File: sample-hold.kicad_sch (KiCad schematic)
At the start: 76 parts, among them J1 Conn_02x05_Odd_Even, J2 AudioJack2_SwitchT, J3 AudioJack2_SwitchT, J4 AudioJack2_SwitchT, J5 AudioJack2_SwitchT, Q1 BC547C, Q2 BCM847, Q3 MMBF4393, SW1 ON-ON-ON, U1 TL074, U2 TL074

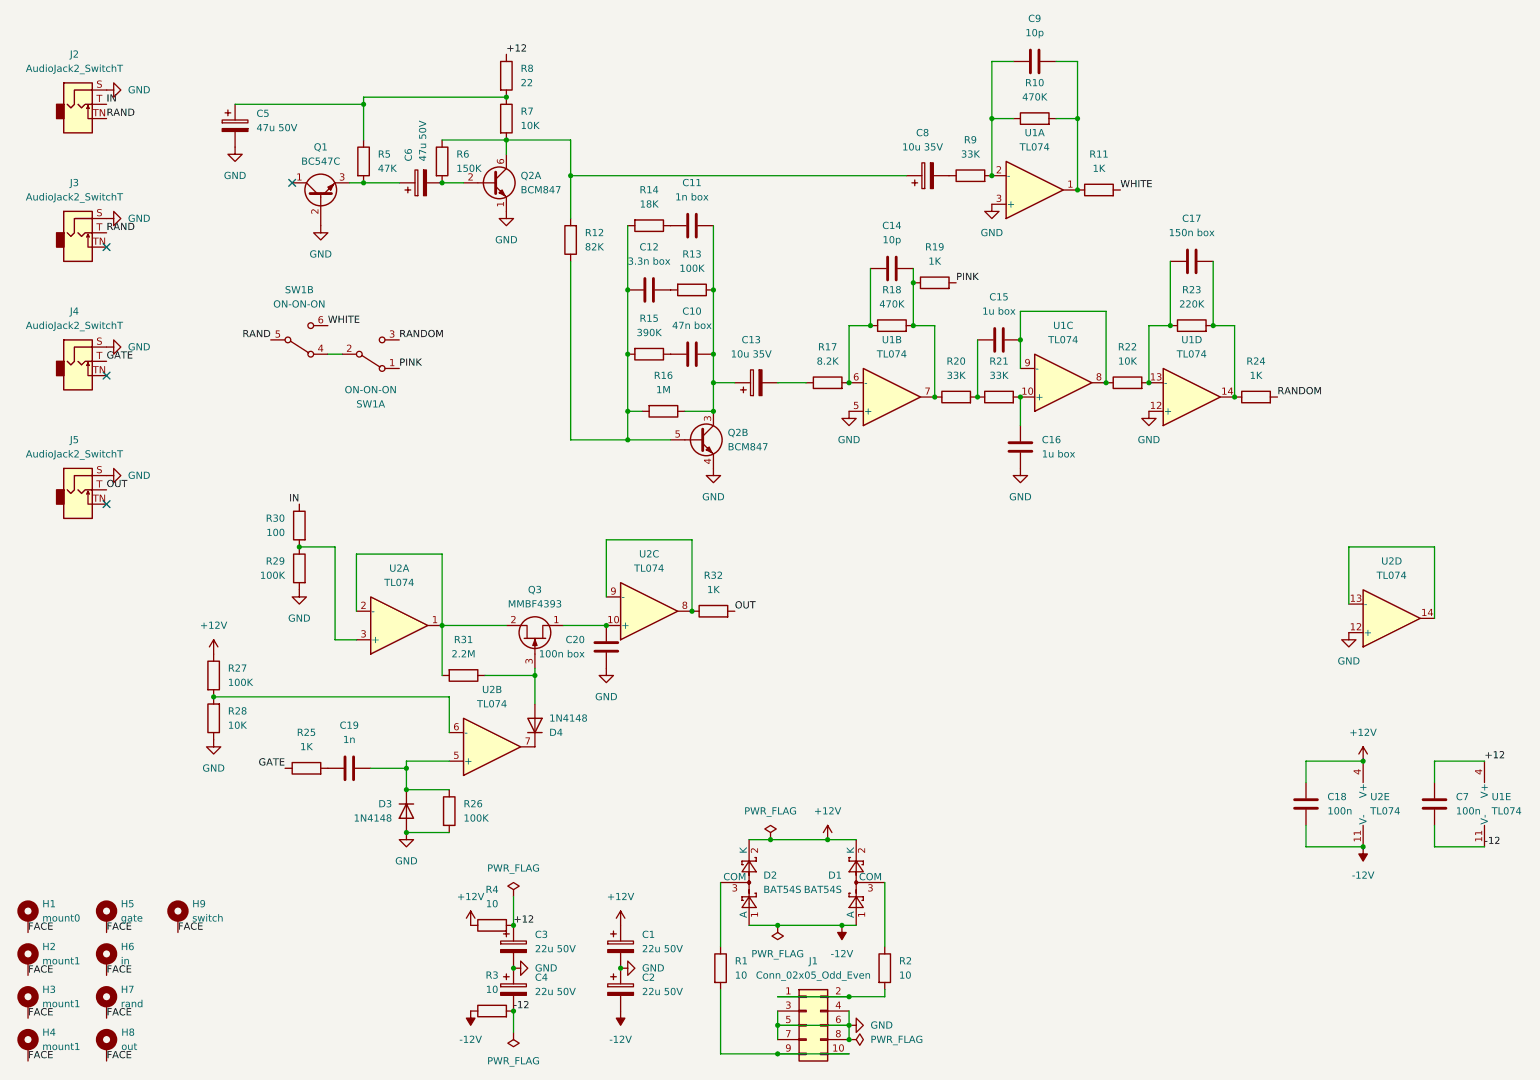
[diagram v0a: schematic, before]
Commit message: adding rate knob and internal clock
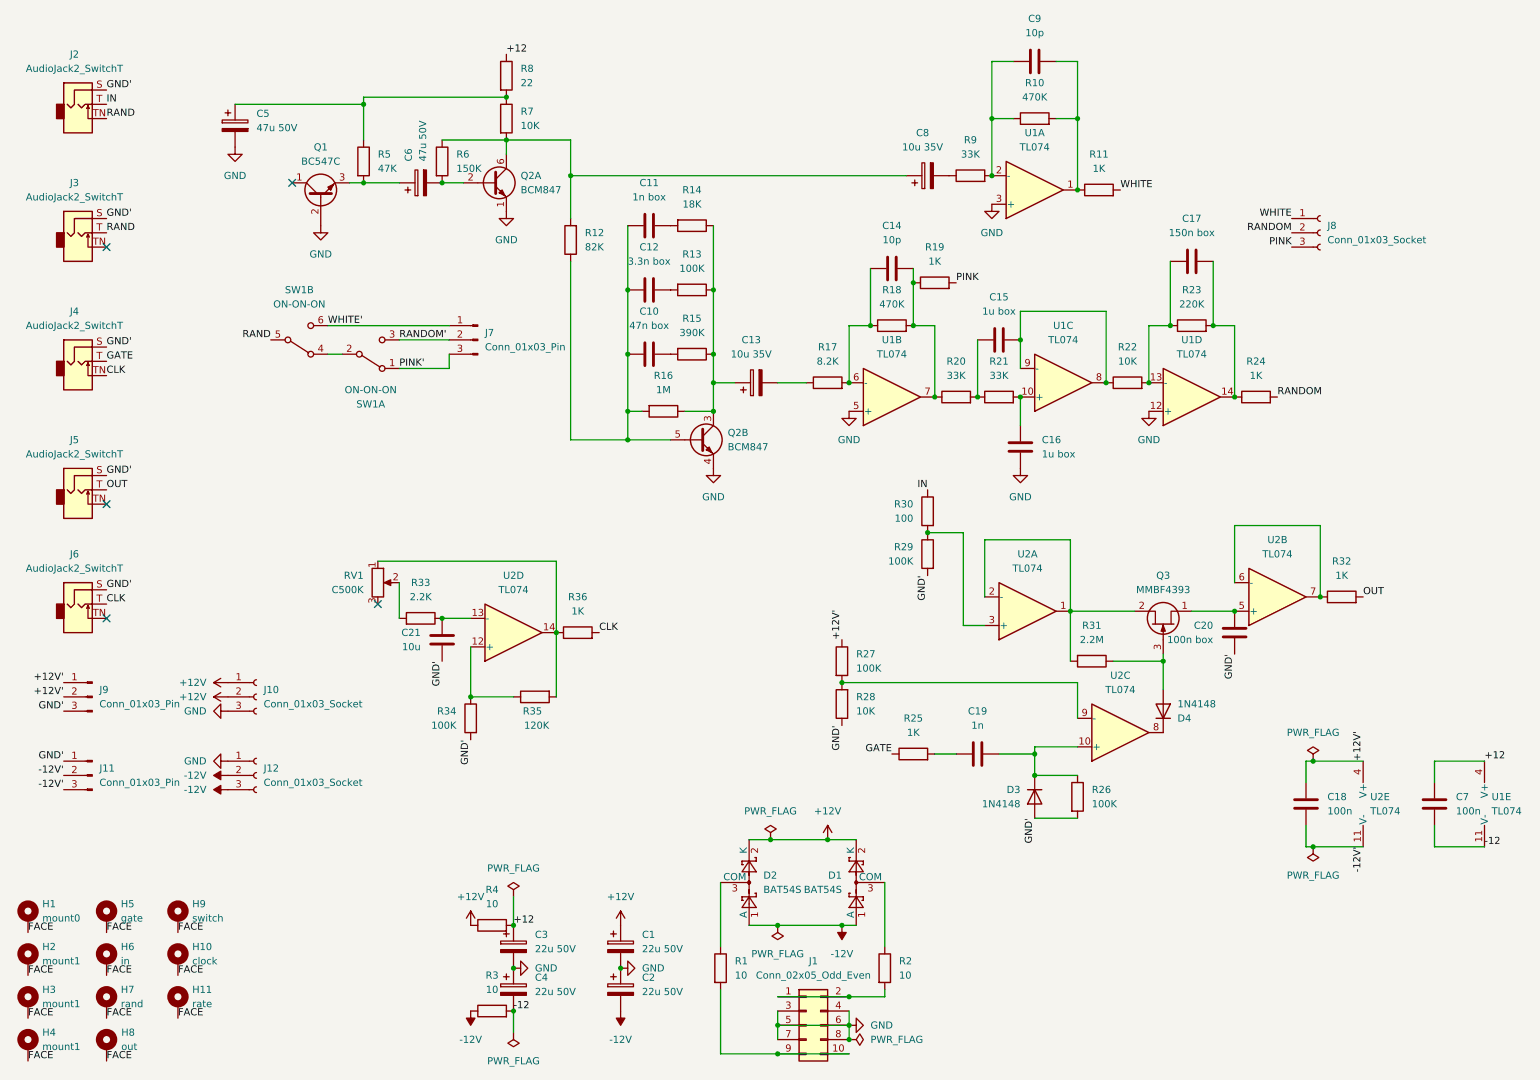
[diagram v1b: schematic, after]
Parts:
- added C21: 10u, Capacitor_SMD:C_0805_2012Metric, symbol Device:C
- added H10: clock, Eurorack:Mech-AudioJack-Hole-Output-Clock, symbol Mechanical:MountingHole_Pad
- added H11: rate, Eurorack:Mech-Potentiometer-Hole_level_90deg, symbol Mechanical:MountingHole_Pad
- added J10, J12, J8: Conn_01x03_Socket, Connector_PinSocket_2.54mm:PinSocket_1x03_P2.54mm_Vertical, symbol Connector:Conn_01x03_Socket
- added J11, J7, J9: Conn_01x03_Pin, Connector_PinHeader_2.54mm:PinHeader_1x03_P2.54mm_Vertical, symbol Connector:Conn_01x03_Pin
- added J6: AudioJack2_SwitchT, Eurorack:AudioJack2_Tayda_A-2566, symbol Eurorack:AudioJack2_SwitchT
- added R33: 2.2K, Resistor_SMD:R_0805_2012Metric, symbol Device:R
- added R34: 100K, Resistor_SMD:R_0805_2012Metric, symbol Device:R
- added R35: 120K, Resistor_SMD:R_0805_2012Metric, symbol Device:R
- added R36: 1K, Resistor_SMD:R_0805_2012Metric, symbol Device:R
- added RV1: C500K, Eurorack:Potentiometer_RV16AF-41-15R1, symbol Device:R_Potentiometer
- C11: footprint Capacitor_THT:C_Rect_L7.2mm_W5.5mm_P5.00mm_FKS2_FKP2_MKS2_MKP2 -> Capacitor_THT:C_Rect_L7.2mm_W2.5mm_P5.00mm_FKS2_FKP2_MKS2_MKP2
- C20: footprint Capacitor_THT:C_Rect_L7.2mm_W3.5mm_P5.00mm_FKS2_FKP2_MKS2_MKP2 -> Capacitor_THT:C_Rect_L7.2mm_W2.5mm_P5.00mm_FKS2_FKP2_MKS2_MKP2
- H5: footprint Eurorack:Mech-MountingHole -> Eurorack:Mech-AudioJack-Hole-Input-Gate
- H6: footprint Eurorack:Mech-MountingHole -> Eurorack:Mech-AudioJack-Hole-Input-Voct
- H7, H8: footprint Eurorack:Mech-MountingHole -> Eurorack:Mech-AudioJack-Hole-Output-Voct
- H9: footprint Eurorack:Mech-MountingHole -> Eurorack:Mech-2M_Switch-Hole
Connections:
- net +12V: now also J10.1 (Pin_1), J10.2 (Pin_2); no longer C18.1, R27.1, U2.4 (V+)
- net -12V: now also J12.2 (Pin_2), J12.3 (Pin_3); no longer C18.2, U2.11 (V-)
- net FACE: now also H10.1, H11.1
- net GND: now also J10.3 (Pin_3), J12.1 (Pin_1); no longer C20.2, D3.2 (A), J2.S, J3.S, J4.S, J5.S, R26.2, R28.1, R29.2, U2.12 (+)
- net PINK: now also J8.3 (Pin_3); no longer SW1.1 (A)
- net RANDOM: now also J8.2 (Pin_2); no longer SW1.3 (C)
- net WHITE: now also J8.1 (Pin_1); no longer SW1.6 (C)
- net at C13.1, Q2.3 (C2), R13.1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: now also R14.1, R15.1; no longer C10.2, C11.2
- net at C12.1, Q2.5 (B2), R12.1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: now also C10.1, C11.1; no longer R14.2, R15.2
- net CLK: now reaches J4.TN
- net CLK: now also J6.T, R36.2
- net at R27.2, R28.2: now also U2.9 (-); no longer U2.6 (-)
- net at C19.2, D3.1 (K), R26.1: now also U2.10 (+); no longer U2.5 (+)
- net at U2.7: now also R32.1, U2.6 (-); no longer D4.1 (K)
- net at C20.1, Q3.1 (D): now also U2.5 (+); no longer U2.10 (+)
- net at U2.14: now also R35.2, R36.1, RV1.1; no longer U2.13 (-)
- new net: R34.1, R35.1, U2.12 (+)
- new net: C10.2, R15.2
- new net: R33.2, RV1.2
- new net: C11.2, R14.2
- new net: C21.1, R33.1, U2.13 (-)
- new net: D4.1 (K), U2.8
- new net +12V': C18.1, J9.1 (Pin_1), J9.2 (Pin_2), R27.1, U2.4 (V+)
- new net -12V': C18.2, J11.2 (Pin_2), J11.3 (Pin_3), U2.11 (V-)
- new net GND': C20.2, C21.2, D3.2 (A), J11.1 (Pin_1), J2.S, J3.S, J4.S, J5.S, J6.S, J9.3 (Pin_3), R26.2, R28.1, R29.2, R34.2
- new net PINK': J7.3 (Pin_3), SW1.1 (A)
- new net RANDOM': J7.2 (Pin_2), SW1.3 (C)
- new net WHITE': J7.1 (Pin_1), SW1.6 (C)
- no-connect marks 4 -> 5
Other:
- moved on the sheet: C10, C11, C19, C20, D3, D4, Q3, R14, R15, R25, R26, R27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

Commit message: correct capacitor type
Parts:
- removed C21: 10u, Capacitor_SMD:C_0805_2012Metric, symbol Device:C
- added C21: 10u 35V, Capacitor_THT:CP_Radial_D5.0mm_P2.50mm, symbol Device:C_Polarized
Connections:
- net GND': now also C21.2
- net at R33.1, U2.13 (-): now also C21.1
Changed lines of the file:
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@@
   (junction (at 177.8 77.47) (diameter 0) (color 0 0 0 0)
   )
+  (junction (at 90.17 116.84) (diameter 0) (color 0 0 0 0)
+  )
   (junction (at 113.03 38.1) (diameter 0) (color 0 0 0 0)
   )
@@
   )
   (junction (at 187.96 27.94) (diameter 0) (color 0 0 0 0)
-  )
-  (junction (at 90.17 116.84) (diameter 0) (color 0 0 0 0)
   )
   (junction (at 162.56 191.77) (diameter 0) (color 0 0 0 0)
@@
         (path "/54607e40-577c-4def-b17c-96859aef0795"
           (reference "J9") (unit 1)
+        )
+      )
+    )
+  )
+  (symbol (lib_id "Device:C_Polarized") (at 90.17 120.65 0) (mirror y) (unit 1)
+    (in_bom yes) (on_board yes) (dnp no)
+    (property "Reference" "C21" (at 86.36 118.491 0)
+      (effects (font (size 1.27 1.27)) (justify left))
+    )
+    (property "Value" "10u 35V" (at 86.36 121.031 0)
+      (effects (font (size 1.27 1.27)) (justify left))
+    )
+    (property "Footprint" "Capacitor_THT:CP_Radial_D5.0mm_P2.50mm" (at 89.2048 124.46 0)
+      (effects (font (size 1.27 1.27)) hide)
+    )
+    (property "Datasheet" "~" (at 90.17 120.65 0)
+      (effects (font (size 1.27 1.27)) hide)
+    )
+    (pin "1")
+    (pin "2")
+    (instances
+      (project "sample-hold"
+        (path "/54607e40-577c-4def-b17c-96859aef0795"
+          (reference "C21") (unit 1)
         )
       )
@@
         )
       )
-    )
-  )
-  (symbol (lib_id "Device:C") (at 90.17 120.65 0) (unit 1)
-    (in_bom yes) (on_board yes) (dnp no)
-    (property "Reference" "C21" (at 86.36 119.38 0)
-      (effects (font (size 1.27 1.27)) (justify right))
-    )
-    (property "Value" "10u" (at 86.36 121.92 0)
-      (effects (font (size 1.27 1.27)) (justify right))
-    )
-    (property "Footprint" "Capacitor_SMD:C_0805_2012Metric" (at 91.1352 124.46 0)
-      (effects (font (size 1.27 1.27)) hide)
-    )
-    (property "Datasheet" "~" (at 90.17 120.65 0)
-      (effects (font (size 1.27 1.27)) hide)
-    )
-    (pin "2")
-    (pin "1")
-    (instances
-      (project "sample-hold"
-        (path "/54607e40-577c-4def-b17c-96859aef0795"
-          (reference "C21") (unit 1)
-        )
-      )

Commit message: prototype tested and updates made ready for v0 manu
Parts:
- added D5: 1N4148, Diode_SMD:D_SOD-323_HandSoldering, symbol Device:D
- added R37, R38, R39, R40: 100K, Resistor_SMD:R_0805_2012Metric, symbol Device:R
- added R41: 3.9K, Resistor_SMD:R_0805_2012Metric, symbol Device:R
- added R42: 24K, Resistor_SMD:R_0805_2012Metric, symbol Device:R
- added R43: 33K, Resistor_SMD:R_0805_2012Metric, symbol Device:R
- Q3: value MMBF4393 -> MMBFJ111
- R30: value 100 -> 100K
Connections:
- net +12: now also R41.1
- net +12V': now also R43.1
- net -12V': now also C21.2
- net GND': now also R40.1, R42.2; no longer C21.2
- net at C13.1, Q2.3 (C2), R13.1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: now also R41.2
- net at R29.1, R30.2: now also R37.1; no longer U2.3 (+)
- net at R35.2, U2.14: now also RV1.3, D5.2 (A); no longer R36.1, RV1.1
- net at Q3.2 (S), R31.2, U2.1: now also R39.1; no longer U2.2 (-)
- new net: R39.2, R40.2, U2.2 (-)
- new net: D5.1 (K), R36.1
- new net: R37.2, R38.1, U2.3 (+)
- new net: R38.2, R42.1, R43.2
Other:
- moved on the sheet: R29, R30, R36
